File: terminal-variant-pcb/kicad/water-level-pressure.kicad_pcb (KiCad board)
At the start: 2 copper layers, 93.3 x 60.1 mm, 40 parts, among them J1 Conn_01x03, J2 Conn_01x04, J3 Conn_01x02, J4 Conn_01x15_Socket, J5 Conn_01x15_Socket, T1 TestPoint, T10 TestPoint, T11 TestPoint, T12 TestPoint, T13 TestPoint, T14 TestPoint, T15 TestPoint, T16 TestPoint, T17 TestPoint, T18 TestPoint, T19 TestPoint, T2 TestPoint, T20 TestPoint, T21 TestPoint, T22 TestPoint, T23 TestPoint, T24 TestPoint, T25 TestPoint, T26 TestPoint, T27 TestPoint, T28 TestPoint, T29 TestPoint, T3 TestPoint, T30 TestPoint, T4 TestPoint, T5 TestPoint, T6 TestPoint, T7 TestPoint, T8 TestPoint, T9 TestPoint

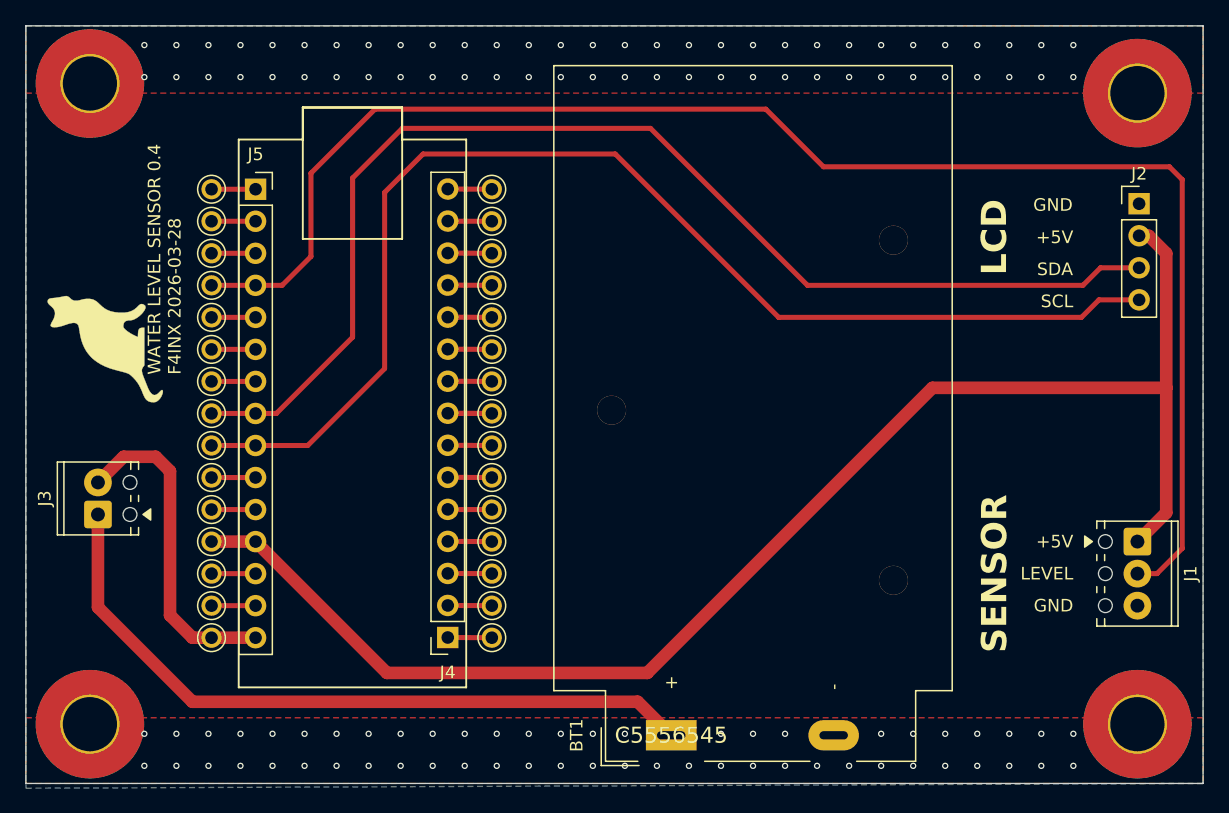
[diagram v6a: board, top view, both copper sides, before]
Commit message: Version 0.5. Fix connectors orientation. Fix title in schematic (was title of old version using ultrasonic). Fix pads footprints paths (was old ultrasonic).
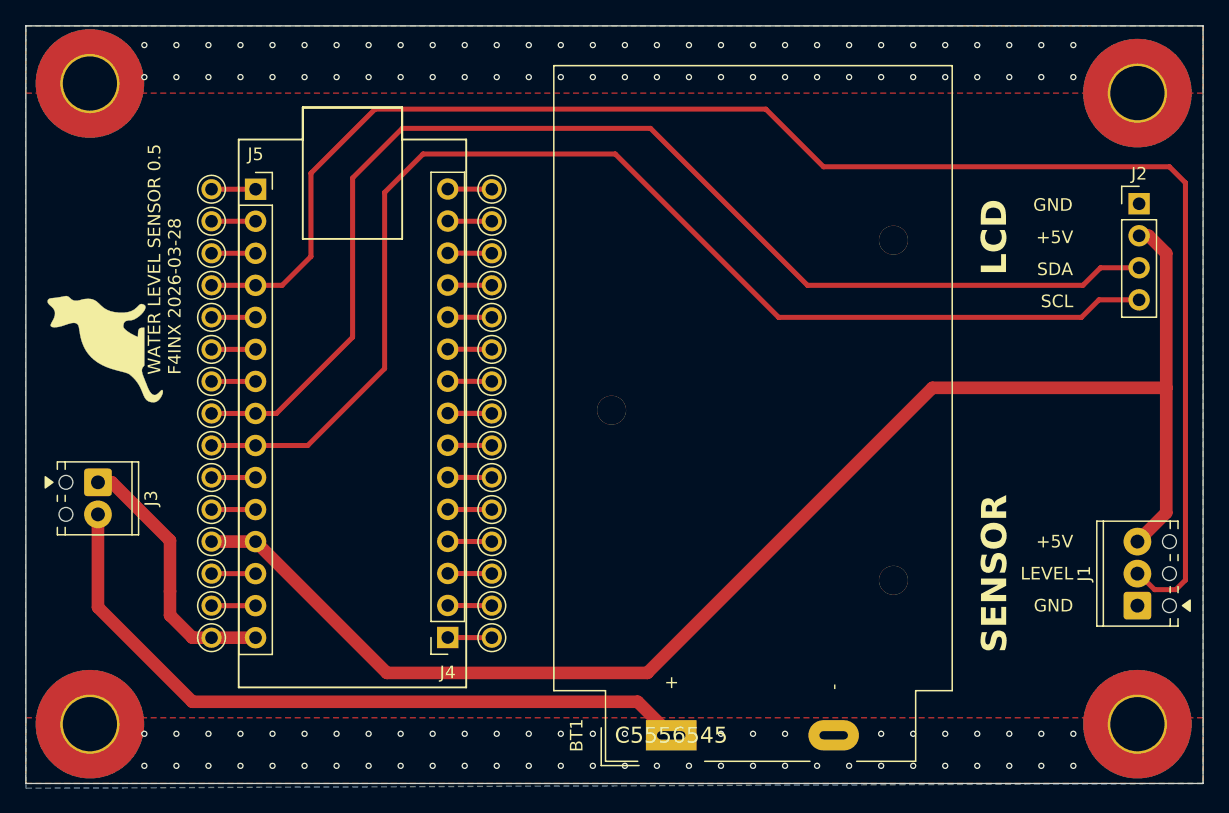
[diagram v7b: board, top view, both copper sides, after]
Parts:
- T1, T10, T11, T12, T13, T14, T15, T16, T17, T18, T19, T2, T20, T21, T22, T23, T24, T25, T26, T27, T28, T29, T3, T30, T4, T5, T6, T7, T8, T9: footprint ultrasonic-pcb:TestPoint_THTPad_D1.6mm_Drill1.0mm_Variant -> water-level-pressure:TestPoint_THTPad_D1.6mm_Drill1.0mm_Variant
- moved J1 5.08 mm to (205.0, 127.8), turned to 90 degrees
- moved J3 2.55 mm to (122.6, 118.0), turned to -90 degrees
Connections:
- J1 pad 1: +5V -> GND
- J1 pad 3: GND -> +5V
- J3 pad 1: /VBAT -> /VIN
- J3 pad 2: /VIN -> /VBAT
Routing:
- net /VIN: track 26.0 -> 21.1 mm
- net /LEVEL: track 122.6 -> 125.4 mm
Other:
- board text added: "WATER LEVEL SENSOR 0.5 F4INX 2026-03-28"
- board text removed: "WATER LEVEL SENSOR 0.4 F4INX 2026-03-28"
